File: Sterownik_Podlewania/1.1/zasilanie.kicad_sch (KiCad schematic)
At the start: 10 parts, among them J1 Barrel_Jack_MountingPin, J15 Screw_Terminal_01x02, U3 L7805, U4 LD1117S33TR_SOT223

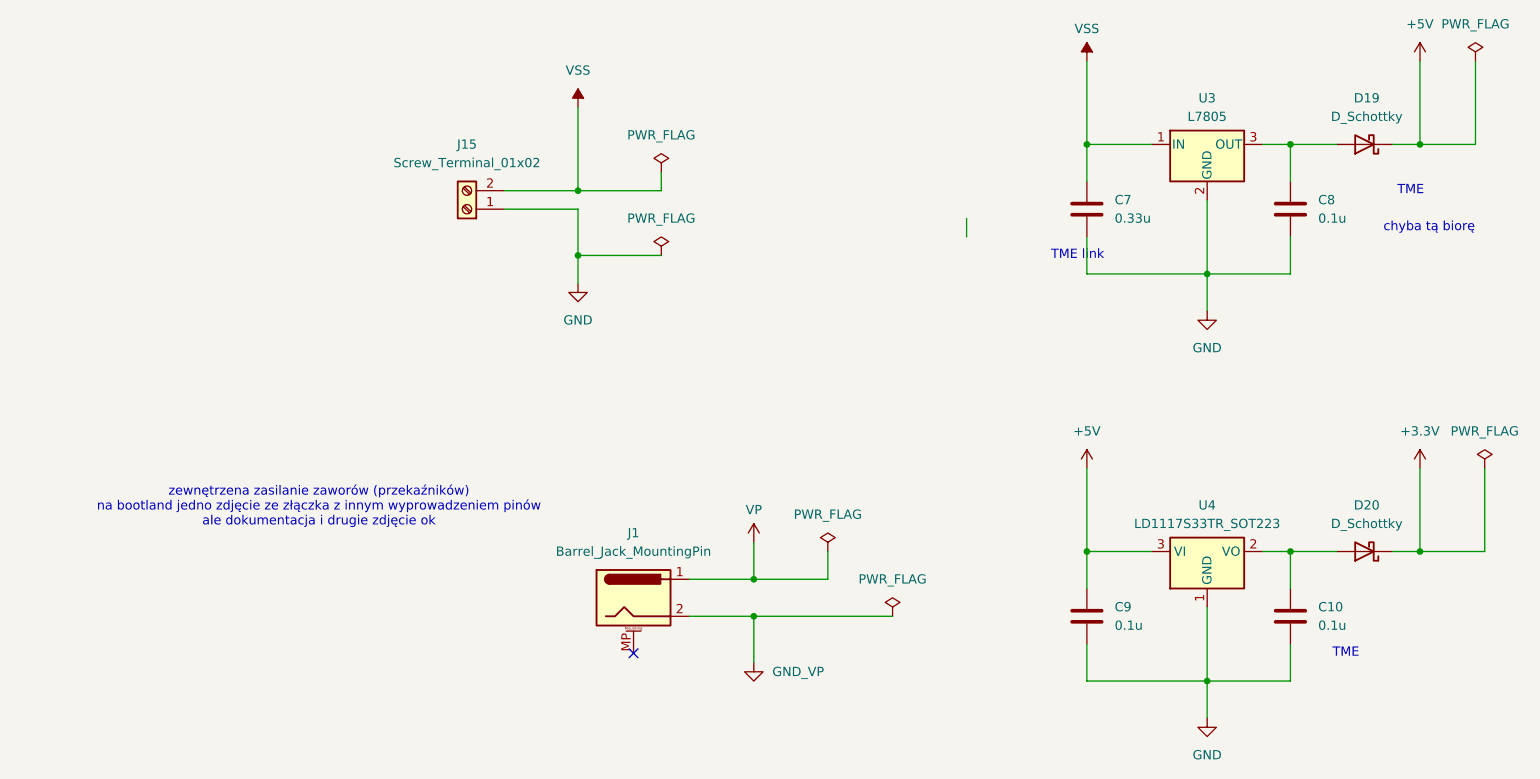
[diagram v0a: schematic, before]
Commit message: Poprawiono błędy połączeń SDA,SCL, dodno drugą magistralę I2C, pociągnięcie nowych ścieżek
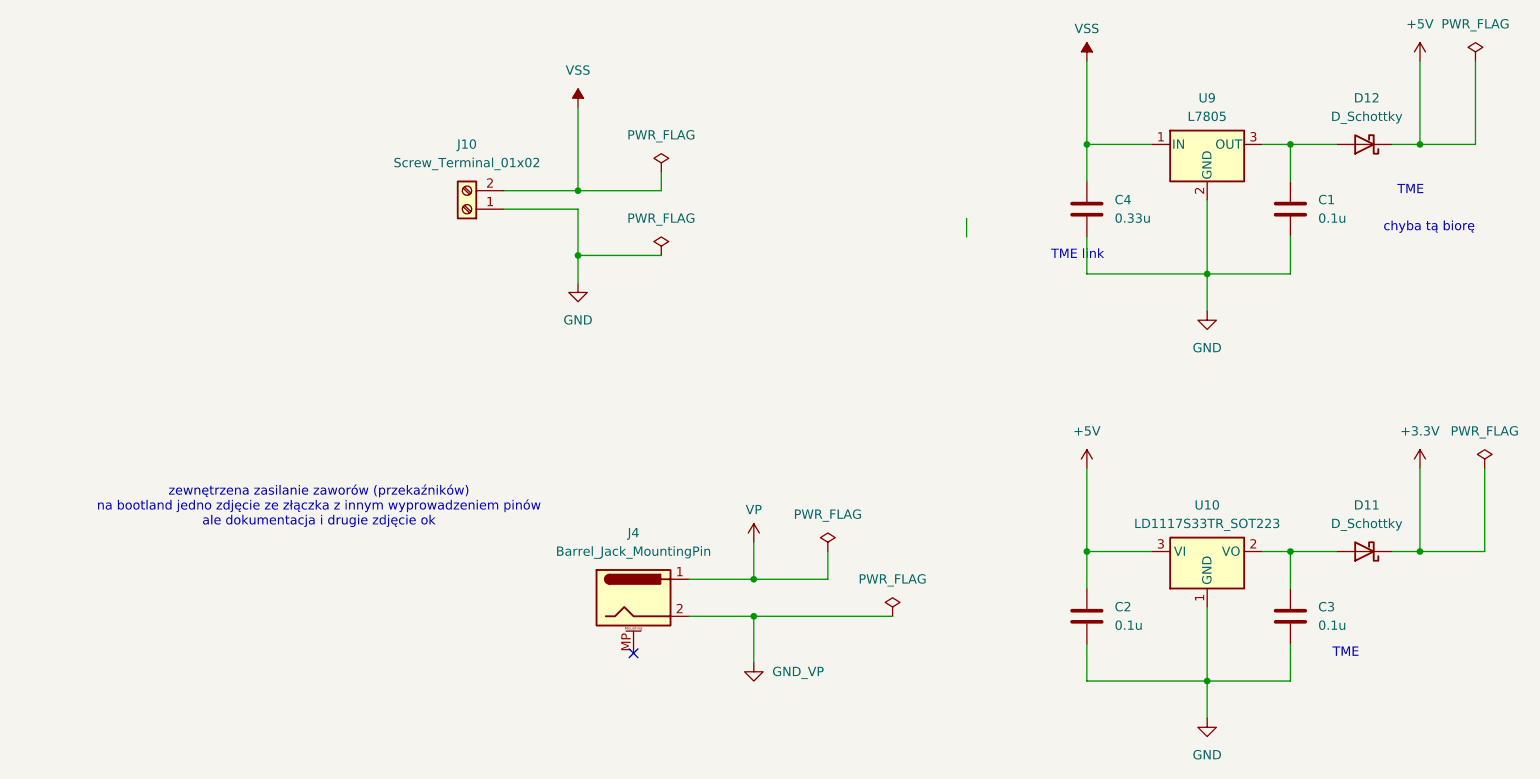
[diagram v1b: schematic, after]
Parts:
- renumbered C8 to C1, C9 to C2, C10 to C3, C7 to C4, D20 to D11, D19 to D12, J15 to J10, J1 to J4, U4 to U10, U3 to U9
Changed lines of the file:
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@@
 		(dnp no)
 		(fields_autoplaced yes)
-		(property "Reference" "J1"
+		(property "Reference" "J4"
 			(at 92.71 106.68 0)
 			(effects
@@
 			(project ""
 				(path "/a66bdf1f-0e2a-4cc5-beb1-605f2a3b9885/73dd885a-a6d0-4e55-a40e-d99ff27ab8ee"
-					(reference "J1")
+					(reference "J4")
 					(unit 1)
 				)
@@
 		(dnp no)
 		(fields_autoplaced yes)
-		(property "Reference" "U3"
+		(property "Reference" "U9"
 			(at 171.45 46.99 0)
 			(effects
@@
 			(project "Sterownik_Podlewania"
 				(path "/a66bdf1f-0e2a-4cc5-beb1-605f2a3b9885/73dd885a-a6d0-4e55-a40e-d99ff27ab8ee"
-					(reference "U3")
+					(reference "U9")
 					(unit 1)
 				)
@@
 		(dnp no)
 		(fields_autoplaced yes)
-		(property "Reference" "C7"
+		(property "Reference" "C4"
 			(at 158.75 60.9599 0)
 			(effects
@@
 			(project "Sterownik_Podlewania"
 				(path "/a66bdf1f-0e2a-4cc5-beb1-605f2a3b9885/73dd885a-a6d0-4e55-a40e-d99ff27ab8ee"
-					(reference "C7")
+					(reference "C4")
 					(unit 1)
 				)
@@
 		(dnp no)
 		(fields_autoplaced yes)
-		(property "Reference" "C10"
+		(property "Reference" "C3"
 			(at 186.69 116.8399 0)
 			(effects
@@
 			(project "Sterownik_Podlewania"
 				(path "/a66bdf1f-0e2a-4cc5-beb1-605f2a3b9885/73dd885a-a6d0-4e55-a40e-d99ff27ab8ee"
-					(reference "C10")
+					(reference "C3")
 					(unit 1)
 				)
@@
 		(dnp no)
 		(fields_autoplaced yes)
-		(property "Reference" "U4"
+		(property "Reference" "U10"
 			(at 171.45 102.87 0)
 			(effects
@@
 			(project ""
 				(path "/a66bdf1f-0e2a-4cc5-beb1-605f2a3b9885/73dd885a-a6d0-4e55-a40e-d99ff27ab8ee"
-					(reference "U4")
+					(reference "U10")
 					(unit 1)
 				)
@@
 		(dnp no)
 		(fields_autoplaced yes)
-		(property "Reference" "C8"
+		(property "Reference" "C1"
 			(at 186.69 60.9599 0)
 			(effects
@@
 			(project "Sterownik_Podlewania"
 				(path "/a66bdf1f-0e2a-4cc5-beb1-605f2a3b9885/73dd885a-a6d0-4e55-a40e-d99ff27ab8ee"
-					(reference "C8")
+					(reference "C1")
 					(unit 1)
 				)
@@
 		(dnp no)
 		(fields_autoplaced yes)
-		(property "Reference" "J15"
+		(property "Reference" "J10"
 			(at 69.85 53.34 0)
 			(effects
@@
 			(project "Sterownik_Podlewania"
 				(path "/a66bdf1f-0e2a-4cc5-beb1-605f2a3b9885/73dd885a-a6d0-4e55-a40e-d99ff27ab8ee"
-					(reference "J15")
+					(reference "J10")
 					(unit 1)
 				)
@@
 		(dnp no)
 		(fields_autoplaced yes)
-		(property "Reference" "D20"
+		(property "Reference" "D11"
 			(at 193.3575 102.87 0)
 			(effects
@@
 			(project "Sterownik_Podlewania"
 				(path "/a66bdf1f-0e2a-4cc5-beb1-605f2a3b9885/73dd885a-a6d0-4e55-a40e-d99ff27ab8ee"
-					(reference "D20")
+					(reference "D11")
 					(unit 1)
 				)
@@
 		(dnp no)
 		(fields_autoplaced yes)
-		(property "Reference" "C9"
+		(property "Reference" "C2"
 			(at 158.75 116.8399 0)
 			(effects
@@
 			(project "Sterownik_Podlewania"
 				(path "/a66bdf1f-0e2a-4cc5-beb1-605f2a3b9885/73dd885a-a6d0-4e55-a40e-d99ff27ab8ee"
-					(reference "C9")
+					(reference "C2")
 					(unit 1)
 				)
@@
 		(dnp no)
 		(fields_autoplaced yes)
-		(property "Reference" "D19"
+		(property "Reference" "D12"
 			(at 193.3575 46.99 0)
 			(effects
@@
 			(project "Sterownik_Podlewania"
 				(path "/a66bdf1f-0e2a-4cc5-beb1-605f2a3b9885/73dd885a-a6d0-4e55-a40e-d99ff27ab8ee"
-					(reference "D19")
-					(unit 1)
-				)
+					(reference "D12")
+					(unit 1)
+				)

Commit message: Usunięcie zewnętrzego zasilania 12 i stabilizatora napięcia, korekcja zasilania wzmacniacz operacyjny moduł zasilania
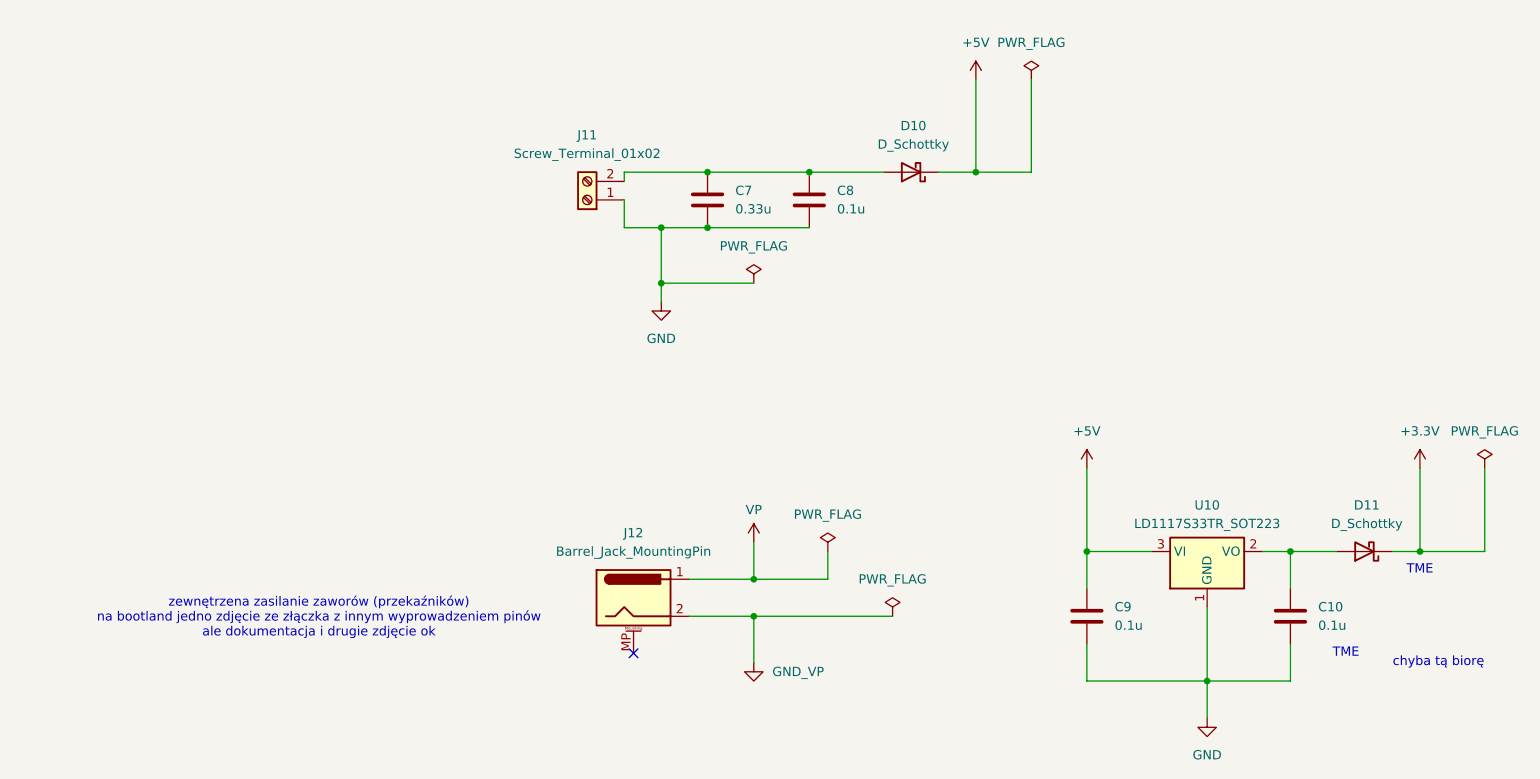
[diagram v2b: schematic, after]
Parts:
- removed C1: 0.1u, Capacitor_THT:C_Disc_D3.0mm_W1.6mm_P2.50mm, symbol Device:C
- removed D12: D_Schottky, Diode_SMD:D_1206_3216Metric, symbol Device:D_Schottky
- removed U9: L7805, Package_TO_SOT_THT:TO-220-3_Vertical, symbol Regulator_Linear:L7805
- added C8: 0.1u, Capacitor_THT:C_Disc_D3.0mm_W1.6mm_P2.50mm, symbol Device:C
- added D10: D_Schottky, Diode_SMD:D_1206_3216Metric, symbol Device:D_Schottky
- renumbered C3 to C10, C4 to C7, C2 to C9, J10 to J11, J4 to J12
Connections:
- net +5V: now also D10.1 (K)
- net GND: now also C8.2
- net VSS: no longer names the net of C7.1, J11.2 (Pin_2)
- net VSS: now also C8.1, D10.2 (A)
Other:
- note removed: "TME link"
- moved on the sheet: C7, J11

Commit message: Werja plików podesłana Mariuszkowi, dodane opisy i numeracja poprawna dla steronwika, w module poprawniono opis złącze ethernet
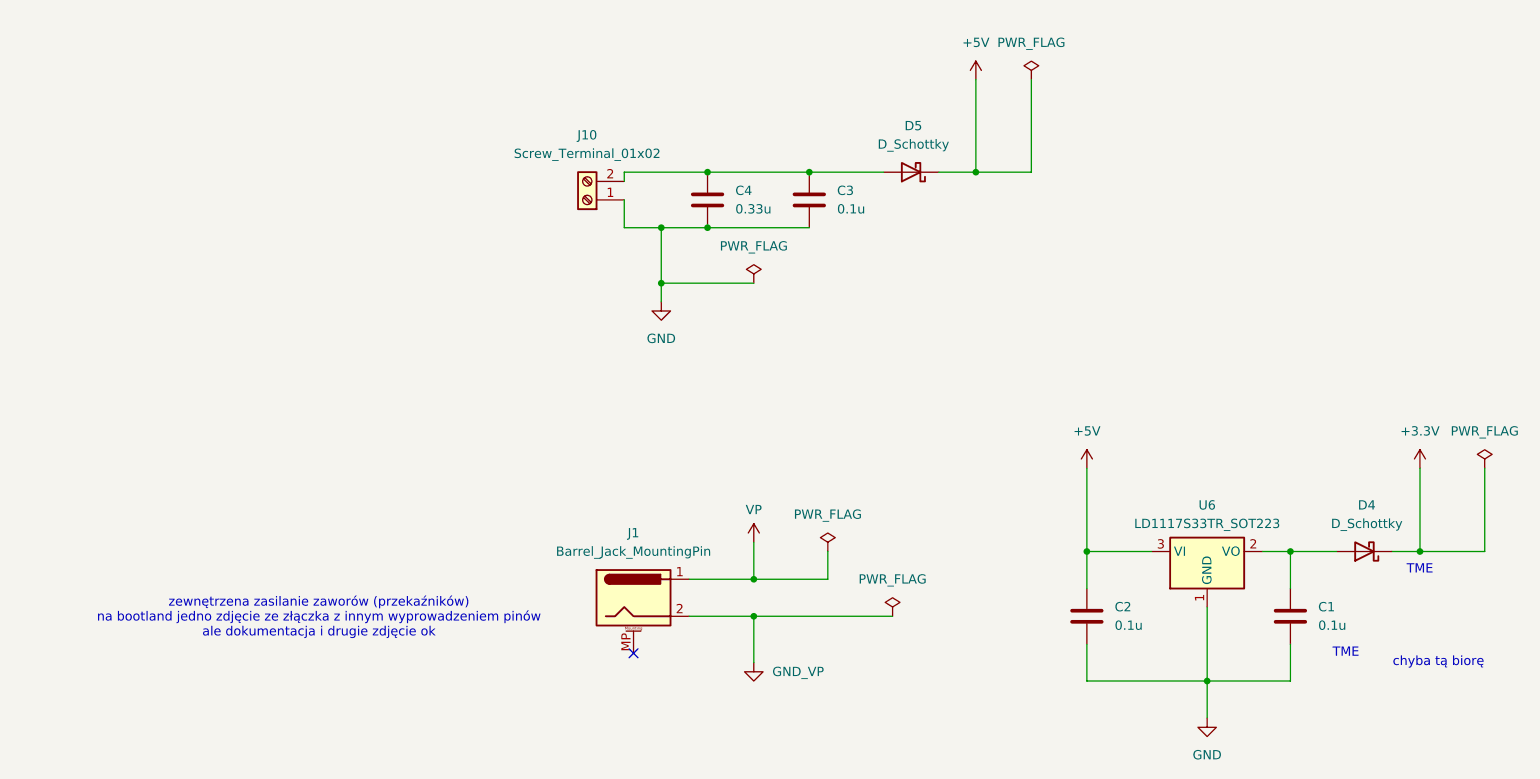
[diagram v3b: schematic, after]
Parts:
- renumbered C10 to C1, C9 to C2, C8 to C3, C7 to C4, D11 to D4, D10 to D5, J12 to J1, J11 to J10, U10 to U6
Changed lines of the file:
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@@
 		(dnp no)
 		(fields_autoplaced yes)
-		(property "Reference" "J12"
+		(property "Reference" "J1"
 			(at 92.71 106.68 0)
 			(effects
@@
 			(project ""
 				(path "/a66bdf1f-0e2a-4cc5-beb1-605f2a3b9885/73dd885a-a6d0-4e55-a40e-d99ff27ab8ee"
-					(reference "J12")
+					(reference "J1")
 					(unit 1)
 				)
@@
 		(dnp no)
 		(fields_autoplaced yes)
-		(property "Reference" "C7"
+		(property "Reference" "C4"
 			(at 106.68 59.6899 0)
 			(effects
@@
 			(project "Sterownik_Podlewania V1.1"
 				(path "/a66bdf1f-0e2a-4cc5-beb1-605f2a3b9885/73dd885a-a6d0-4e55-a40e-d99ff27ab8ee"
-					(reference "C7")
+					(reference "C4")
 					(unit 1)
 				)
@@
 		(dnp no)
 		(fields_autoplaced yes)
-		(property "Reference" "C10"
+		(property "Reference" "C1"
 			(at 186.69 116.8399 0)
 			(effects
@@
 			(project "Sterownik_Podlewania"
 				(path "/a66bdf1f-0e2a-4cc5-beb1-605f2a3b9885/73dd885a-a6d0-4e55-a40e-d99ff27ab8ee"
-					(reference "C10")
+					(reference "C1")
 					(unit 1)
 				)
@@
 		(dnp no)
 		(fields_autoplaced yes)
-		(property "Reference" "U10"
+		(property "Reference" "U6"
 			(at 171.45 102.87 0)
 			(effects
@@
 			(project ""
 				(path "/a66bdf1f-0e2a-4cc5-beb1-605f2a3b9885/73dd885a-a6d0-4e55-a40e-d99ff27ab8ee"
-					(reference "U10")
+					(reference "U6")
 					(unit 1)
 				)
@@
 		(dnp no)
 		(fields_autoplaced yes)
-		(property "Reference" "C8"
+		(property "Reference" "C3"
 			(at 120.65 59.6899 0)
 			(effects
@@
 			(project "Sterownik_Podlewania V1.1"
 				(path "/a66bdf1f-0e2a-4cc5-beb1-605f2a3b9885/73dd885a-a6d0-4e55-a40e-d99ff27ab8ee"
-					(reference "C8")
+					(reference "C3")
 					(unit 1)
 				)
@@
 		(dnp no)
 		(fields_autoplaced yes)
-		(property "Reference" "J11"
+		(property "Reference" "J10"
 			(at 86.36 52.07 0)
 			(effects
@@
 			(project "Sterownik_Podlewania"
 				(path "/a66bdf1f-0e2a-4cc5-beb1-605f2a3b9885/73dd885a-a6d0-4e55-a40e-d99ff27ab8ee"
-					(reference "J11")
+					(reference "J10")
 					(unit 1)
 				)
@@
 		(dnp no)
 		(fields_autoplaced yes)
-		(property "Reference" "D11"
+		(property "Reference" "D4"
 			(at 193.3575 102.87 0)
 			(effects
@@
 			(project "Sterownik_Podlewania"
 				(path "/a66bdf1f-0e2a-4cc5-beb1-605f2a3b9885/73dd885a-a6d0-4e55-a40e-d99ff27ab8ee"
-					(reference "D11")
+					(reference "D4")
 					(unit 1)
 				)
@@
 		(dnp no)
 		(fields_autoplaced yes)
-		(property "Reference" "C9"
+		(property "Reference" "C2"
 			(at 158.75 116.8399 0)
 			(effects
@@
 			(project "Sterownik_Podlewania"
 				(path "/a66bdf1f-0e2a-4cc5-beb1-605f2a3b9885/73dd885a-a6d0-4e55-a40e-d99ff27ab8ee"
-					(reference "C9")
+					(reference "C2")
 					(unit 1)
 				)
@@
 		(dnp no)
 		(fields_autoplaced yes)
-		(property "Reference" "D10"
+		(property "Reference" "D5"
 			(at 131.1275 50.8 0)
 			(effects
@@
 			(project "Sterownik_Podlewania V1.1"
 				(path "/a66bdf1f-0e2a-4cc5-beb1-605f2a3b9885/73dd885a-a6d0-4e55-a40e-d99ff27ab8ee"
-					(reference "D10")
-					(unit 1)
-				)
+					(reference "D5")
+					(unit 1)
+				)
